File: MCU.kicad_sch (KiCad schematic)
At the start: 27 parts, among them SW1 SW_Push, U1 STM32F429IGTx, Y1 32.768KHz, Y2 25MHz

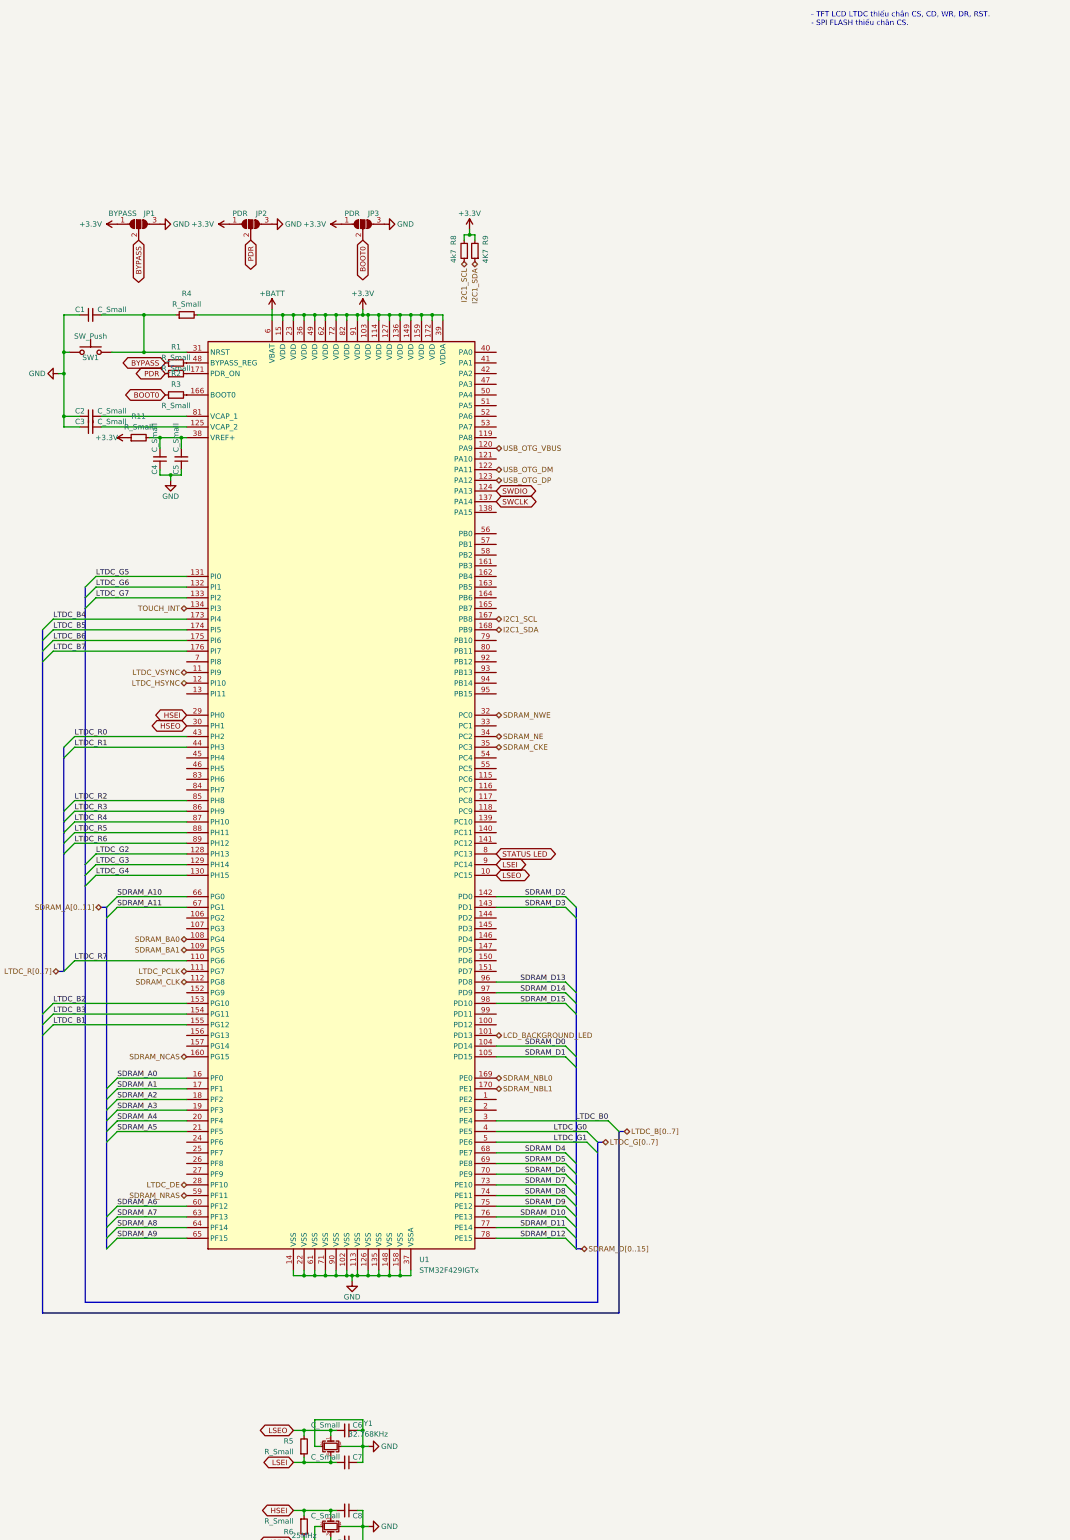
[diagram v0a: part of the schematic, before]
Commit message: Add WiFi block and finished WiFi layout
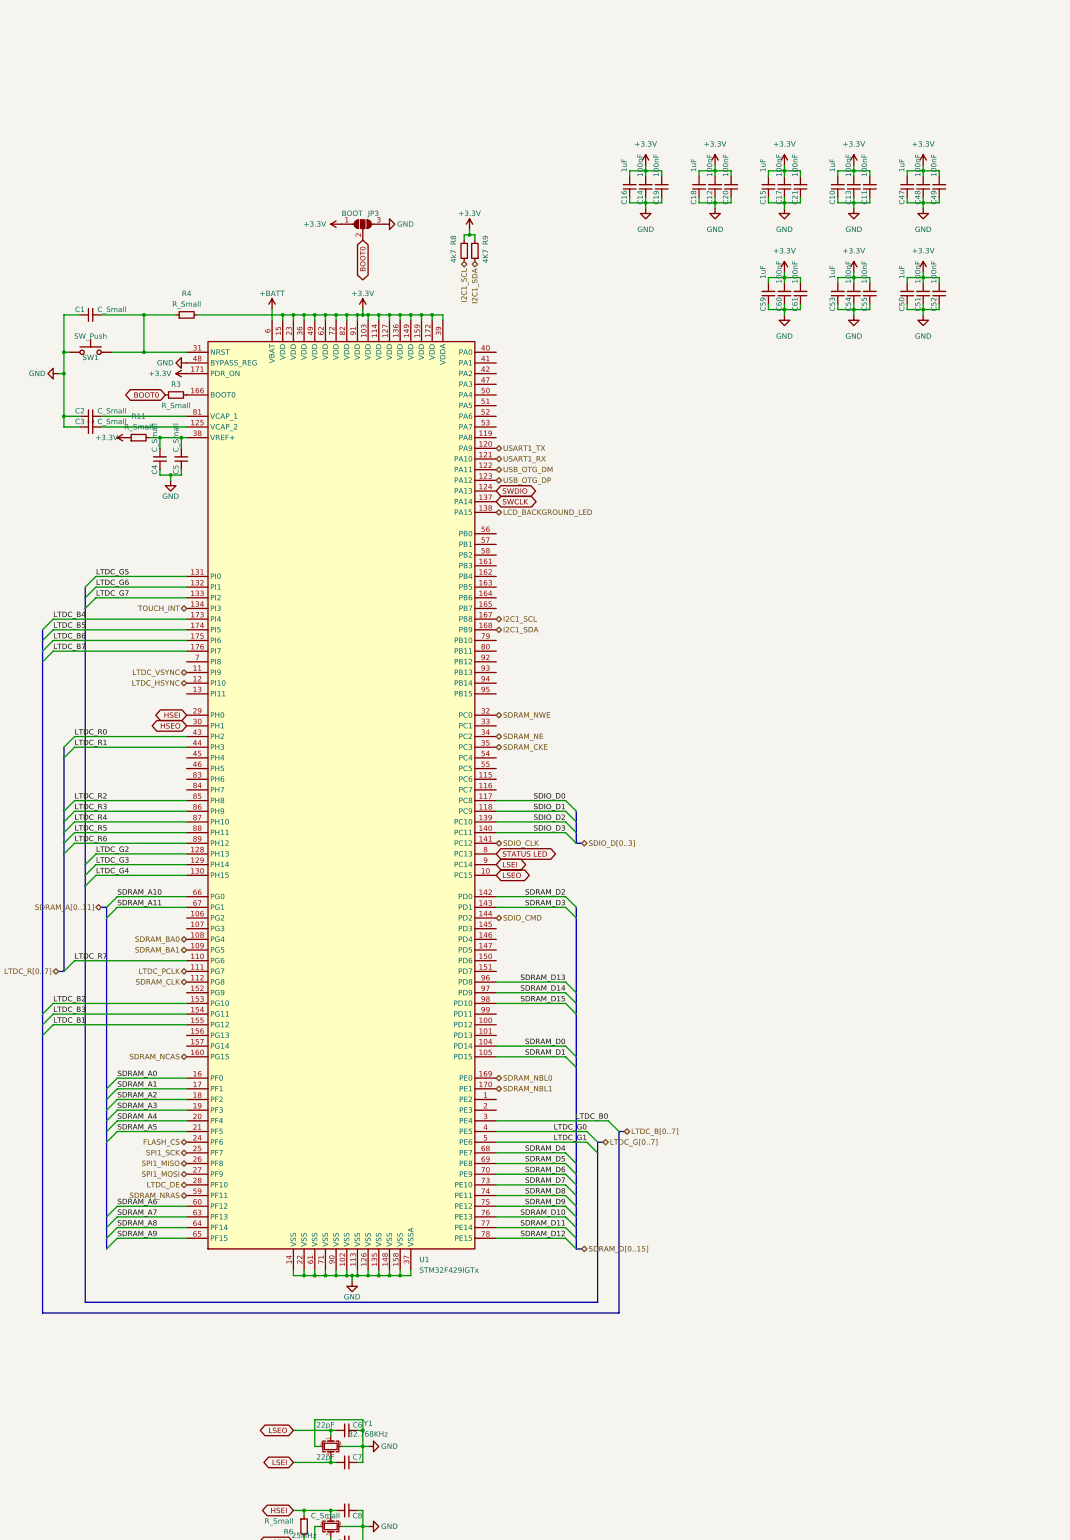
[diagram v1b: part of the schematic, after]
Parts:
- removed JP1: BYPASS, Jumper:SolderJumper-3_P1.3mm_Open_RoundedPad1.0x1.5mm, symbol Jumper:SolderJumper_3_Open
- removed JP2: PDR, Jumper:SolderJumper-3_P1.3mm_Open_RoundedPad1.0x1.5mm, symbol Jumper:SolderJumper_3_Open
- removed R1, R2, R5: R_Small, Resistor_SMD:R_0603_1608Metric, symbol Device:R_Small
- added C10, C15, C16, C18, C47, C50, C53, C59: 1uF, Capacitor_SMD:C_0603_1608Metric, symbol Device:C_Small
- added C11, C12, C13, C14, C17, C19, C20, C21, C48, C49, C51, C52, C54, C55, C60, C61: 100nF, Capacitor_SMD:C_0603_1608Metric, symbol Device:C_Small
- C6, C7: value C_Small -> 22pF
- JP3: value PDR -> BOOT; footprint Jumper:SolderJumper-3_P1.3mm_Open_RoundedPad1.0x1.5mm -> Anh_Footprints:Jump3_0603_Open
- Y2: footprint Crystal:Crystal_SMD_3225-4Pin_3.2x2.5mm_HandSoldering -> Crystal:Crystal_SMD_3225-4Pin_3.2x2.5mm
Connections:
- net +3.3V: now also U1.171 (PDR_ON), C10.2, C11.2, C12.2, C13.2, C14.2, C15.2, C16.2, C17.2, C18.2, C19.2, C20.2, C21.2, C47.2, C48.2, C49.2, C50.2, C51.2, C52.2, C53.2, C54.2, C55.2, C59.2, C60.2, C61.2
- net GND: now also U1.48 (BYPASS_REG), C10.1, C11.1, C12.1, C13.1, C14.1, C15.1, C16.1, C17.1, C18.1, C19.1, C20.1, C21.1, C47.1, C48.1, C49.1, C50.1, C51.1, C52.1, C53.1, C54.1, C55.1, C59.1, C60.1, C61.1
- net LCD_BACKGROUND_LED: now also U1.138 (PA15); no longer U1.101 (PD13)
- net SDIO_D0: now reaches U1.117 (PC8)
- net SDIO_D1: now reaches U1.118 (PC9)
- net USART1_RX: now reaches U1.121 (PA10)
- net SDIO_D2: now reaches U1.139 (PC10)
- net SDIO_D3: now reaches U1.140 (PC11)
- net SDIO_CLK: now reaches U1.141 (PC12)
- net SDIO_CMD: now reaches U1.144 (PD2)
- net FLASH_CS: now reaches U1.24 (PF6)
- net SPI1_SCK: now reaches U1.25 (PF7)
- net SPI1_MISO: now reaches U1.26 (PF8)
- net SPI1_MOSI: now reaches U1.27 (PF9)
- net USB_OTG_VBUS renamed USART1_TX
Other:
- note removed: "- TFT LCD LTDC thiếu chân CS, CD, WR, DR, RST. - SPI FLASH thiếu chân CS."

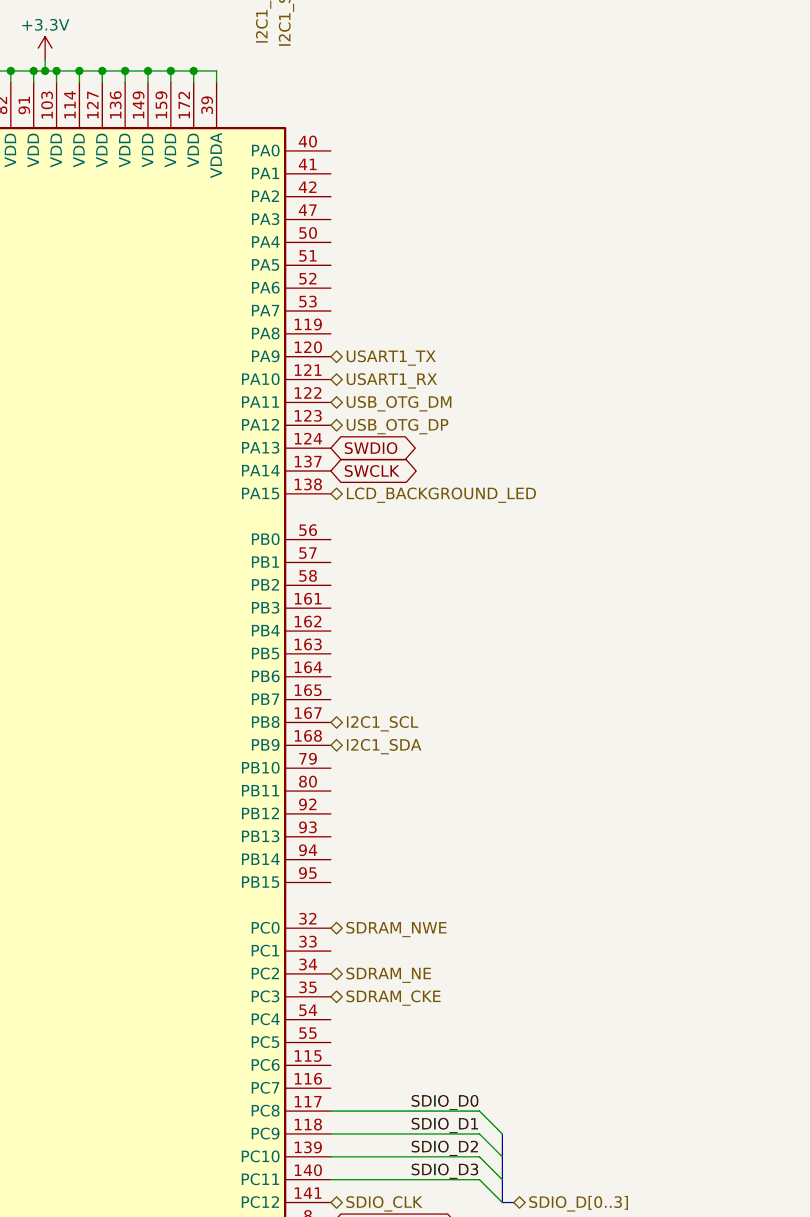
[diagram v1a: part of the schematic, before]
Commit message: Finish Ethernet Layout.
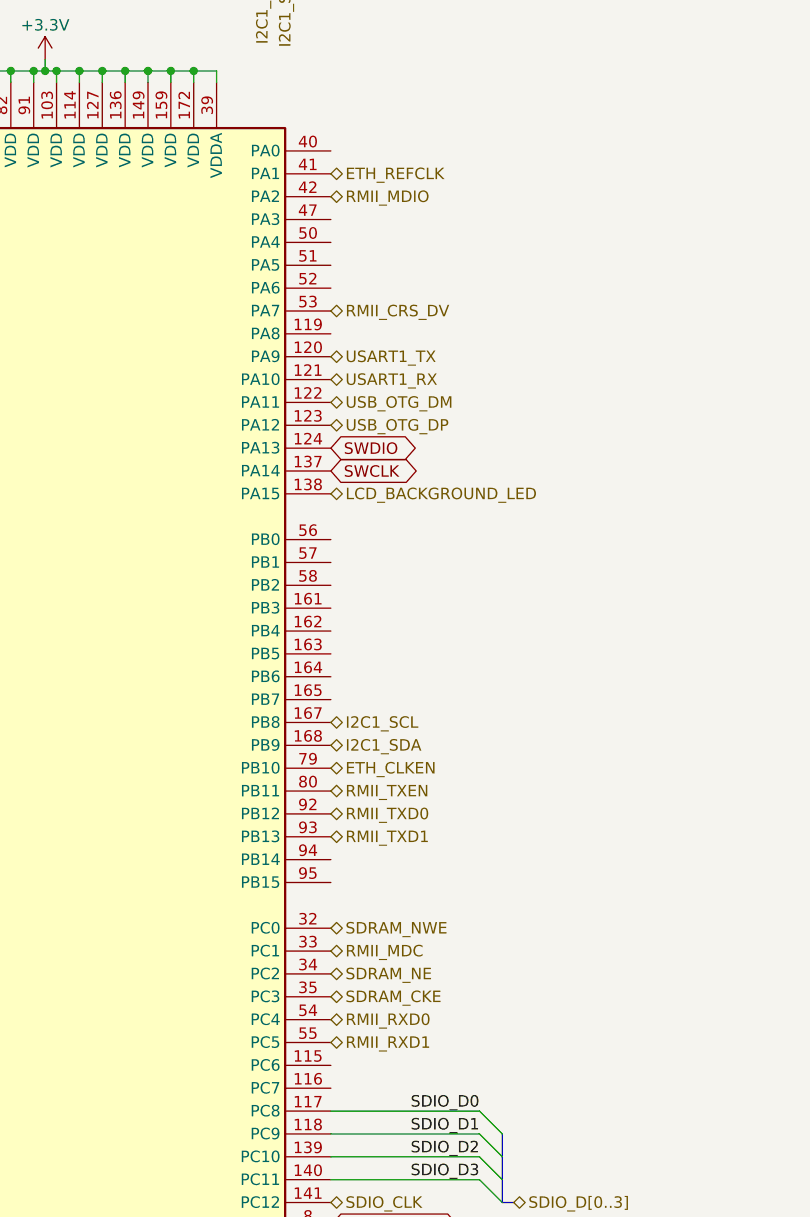
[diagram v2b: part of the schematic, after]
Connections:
- net RMII_MDC: now reaches U1.33 (PC1)
- net ETH_REFCLK: now reaches U1.41 (PA1)
- net RMII_MDIO: now reaches U1.42 (PA2)
- net RMII_CRS_DV: now reaches U1.53 (PA7)
- net RMII_RXD0: now reaches U1.54 (PC4)
- net RMII_RXD1: now reaches U1.55 (PC5)
- net ETH_CLKEN: now reaches U1.79 (PB10)
- net RMII_TXEN: now reaches U1.80 (PB11)
- net RMII_TXD0: now reaches U1.92 (PB12)
- net RMII_TXD1: now reaches U1.93 (PB13)
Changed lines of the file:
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@@
+    (effects (font (size 1.27 1.27)) (justify left))
+  )
+  (hierarchical_label "RMII_MDC" (shape bidirectional) (at 144.78 185.42 0)
     (effects (font (size 1.27 1.27)) (justify left))
   )
@@
     (effects (font (size 1.27 1.27)) (justify left))
   )
+  (hierarchical_label "RMII_TXEN" (shape bidirectional) (at 144.78 167.64 0)
+    (effects (font (size 1.27 1.27)) (justify left))
+  )
+  (hierarchical_label "RMII_RXD1" (shape bidirectional) (at 144.78 195.58 0)
+    (effects (font (size 1.27 1.27)) (justify left))
+  )
+  (hierarchical_label "RMII_CRS_DV" (shape bidirectional) (at 144.78 114.3 0)
+    (effects (font (size 1.27 1.27)) (justify left))
+  )
   (hierarchical_label "LTDC_VSYNC" (shape bidirectional) (at 71.12 172.72 180)
     (effects (font (size 1.27 1.27)) (justify right))
   )
   (hierarchical_label "LCD_BACKGROUND_LED" (shape bidirectional) (at 144.78 134.62 0)
+    (effects (font (size 1.27 1.27)) (justify left))
+  )
+  (hierarchical_label "ETH_REFCLK" (shape bidirectional) (at 144.78 99.06 0)
     (effects (font (size 1.27 1.27)) (justify left))
   )
@@
   (hierarchical_label "SDRAM_NRAS" (shape bidirectional) (at 71.12 297.18 180)
     (effects (font (size 1.27 1.27)) (justify right))
+  )
+  (hierarchical_label "ETH_CLKEN" (shape bidirectional) (at 144.78 165.1 0)
+    (effects (font (size 1.27 1.27)) (justify left))
   )
   (hierarchical_label "LTDC_G[0..7]" (shape bidirectional) (at 170.18 284.48 0)
@@
     (effects (font (size 1.27 1.27)) (justify right))
   )
+  (hierarchical_label "RMII_RXD0" (shape bidirectional) (at 144.78 193.04 0)
+    (effects (font (size 1.27 1.27)) (justify left))
+  )
   (hierarchical_label "LTDC_B[0..7]" (shape bidirectional) (at 175.26 281.94 0)
+    (effects (font (size 1.27 1.27)) (justify left))
+  )
+  (hierarchical_label "RMII_TXD0" (shape bidirectional) (at 144.78 170.18 0)
     (effects (font (size 1.27 1.27)) (justify left))
   )
@@
     (effects (font (size 1.27 1.27)) (justify right))
   )
+  (hierarchical_label "RMII_TXD1" (shape bidirectional) (at 144.78 172.72 0)
+    (effects (font (size 1.27 1.27)) (justify left))
+  )
   (hierarchical_label "I2C1_SDA" (shape bidirectional) (at 139.7 74.93 270)
     (effects (font (size 1.27 1.27)) (justify right))
@@
     (effects (font (size 1.27 1.27)) (justify left))
   )
+  (hierarchical_label "RMII_MDIO" (shape bidirectional) (at 144.78 101.6 0)
+    (effects (font (size 1.27 1.27)) (justify left))
+  )
